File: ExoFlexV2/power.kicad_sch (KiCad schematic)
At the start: 52 parts, among them J1 24V, J2 5V, J3 24V, K1 UD2-5NU, U1 PTSM36ADBZR, U2 PTSM36ADBZR, U3 STPS20M100SG-TR, U4 SN74LVC3G14DCUT_V2, U5 CD4044BPWR, U6 LMZ23603TZ_NOPB, U7 TPS7A4701RGWR

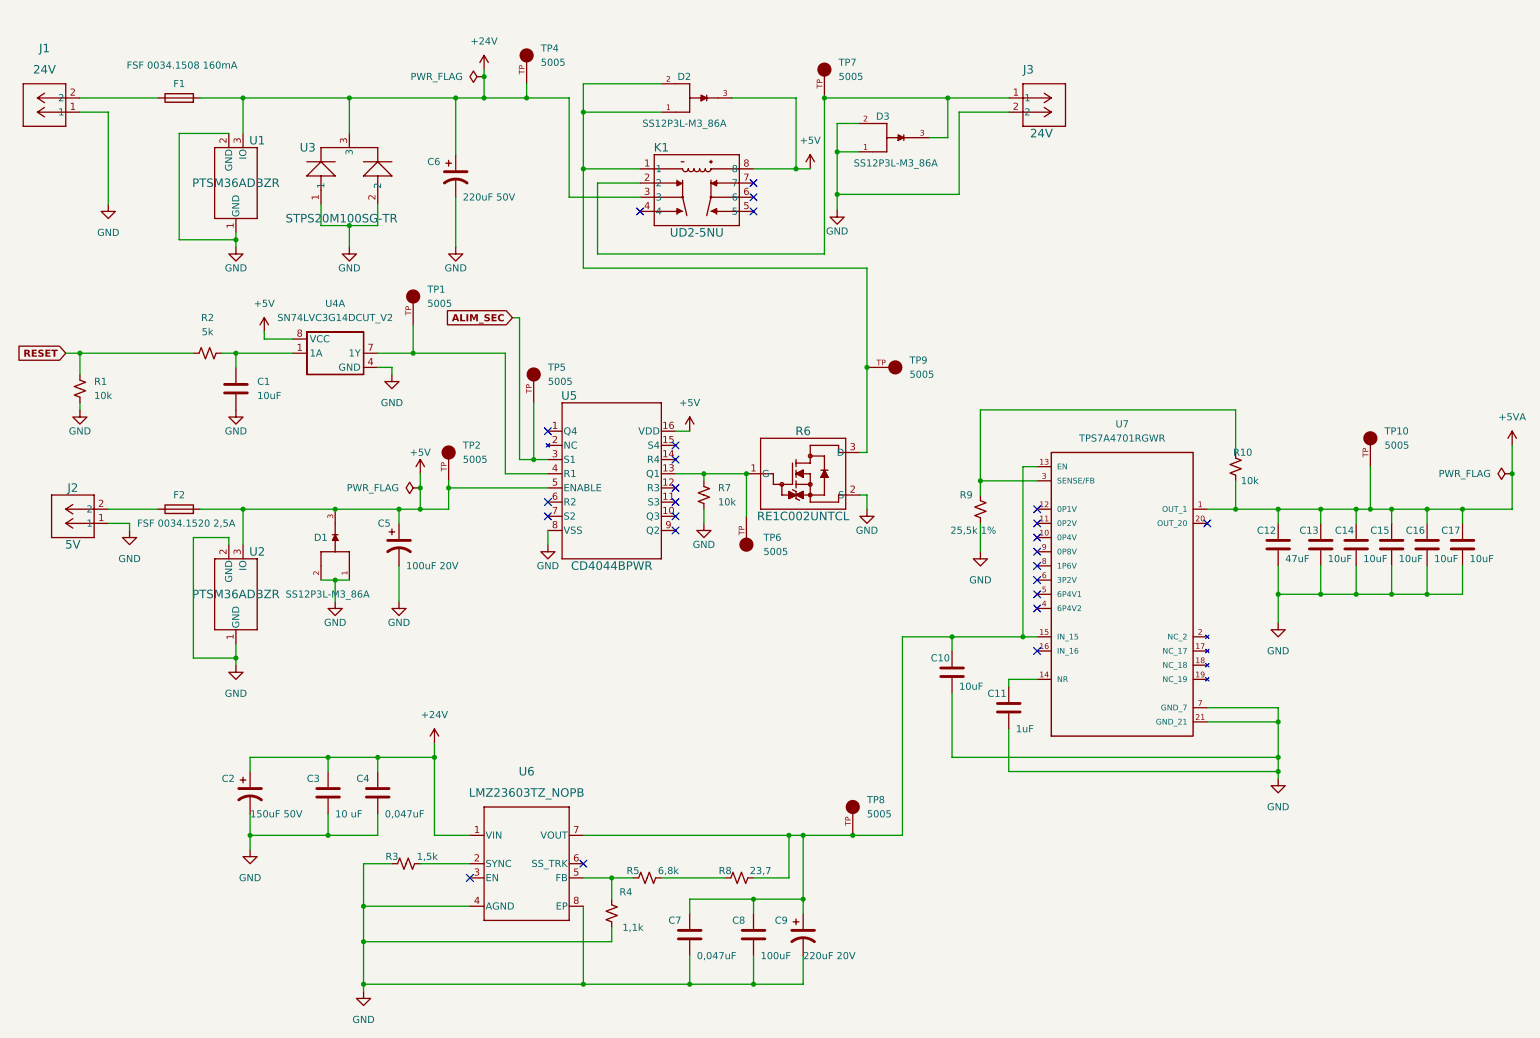
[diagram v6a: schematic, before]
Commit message: Mise à jour signaux STM
- Condo de découplage
- Signaux supplémentaire pour le STM
- Page GND sera pour Multiplexeur
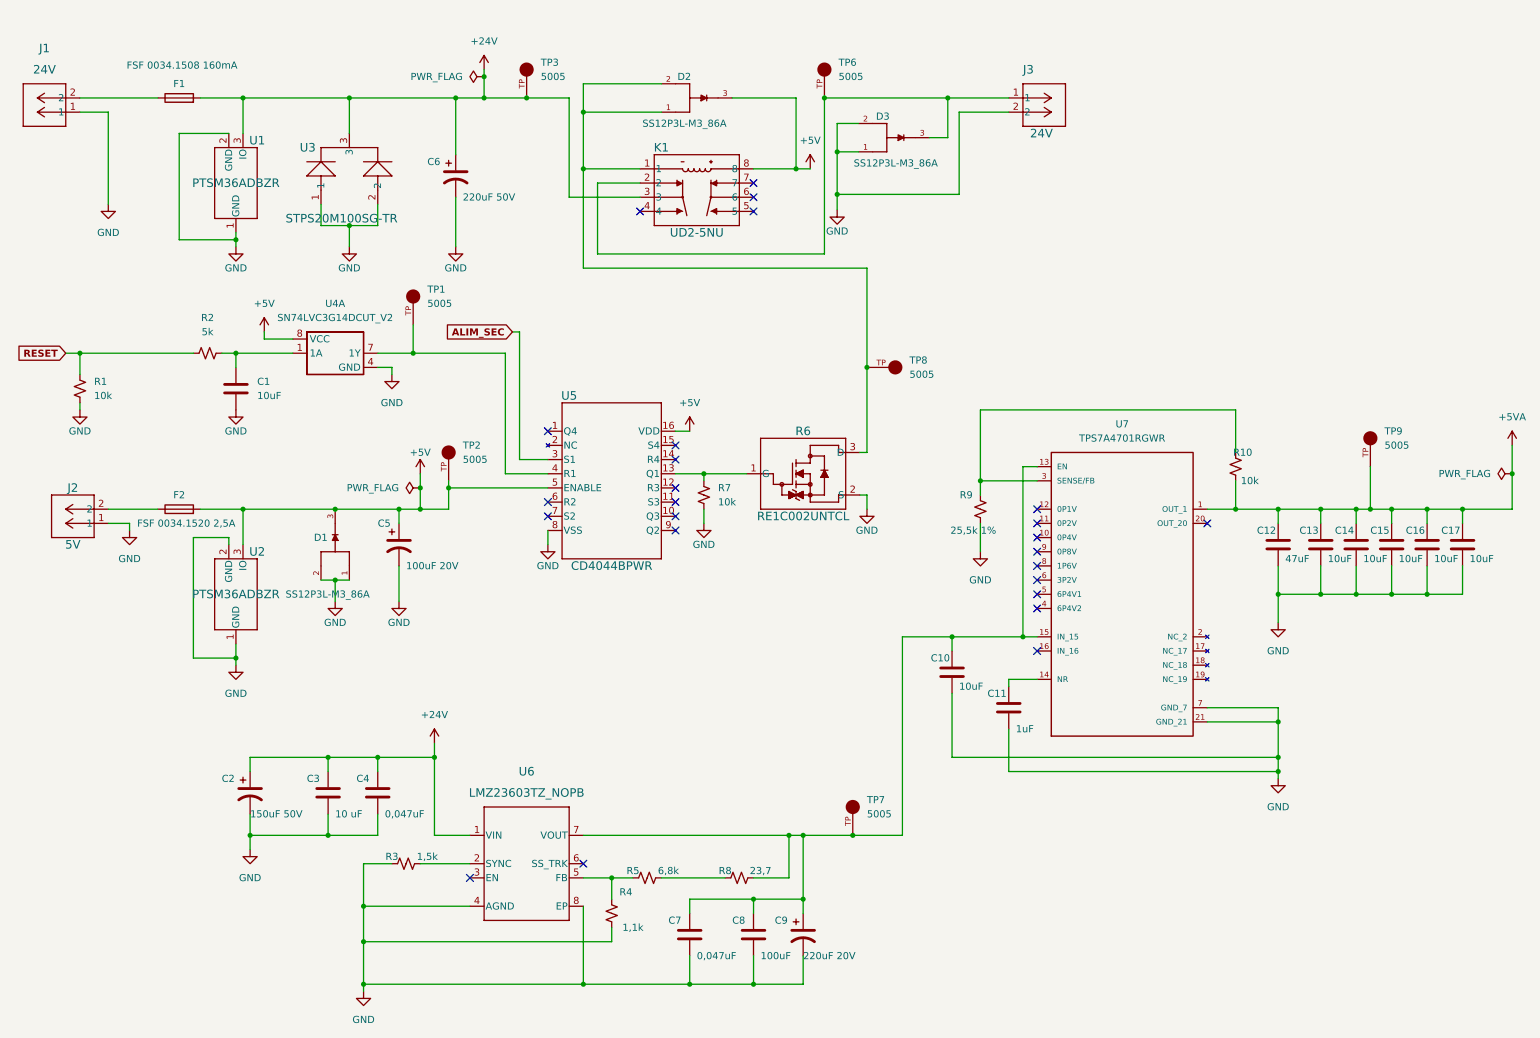
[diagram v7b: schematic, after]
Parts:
- removed TP5, TP6: 5005, FootPrint:KEYSTONE_5005, symbol SymLib:5005
- renumbered TP4 to TP3, TP7 to TP6, TP8 to TP7, TP9 to TP8, TP10 to TP9
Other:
- moved on the sheet: TP3
